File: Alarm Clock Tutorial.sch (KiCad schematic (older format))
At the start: 19 parts, among them K1 DIP-SWITCH-TACTILE-SPST-NO_TS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, K2 DIP-SWITCH-TACTILE-SPST-NO_TS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, K3 DIP-SWITCH-TACTILE-SPST-NO_TS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, U1 MCU-ATMEGA32U4-AU_TQFP44_, U2 LED-4-BETY-7-SEG_2X7P-30X14MM_

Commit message: First version fully routed
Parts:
- added BUZ1: DIP-BUZZER-3V_KS-12065D03YA_, SeeedOPL-Connector-2016:BZ2-7.6-D12.0XH6.5MM, symbol DIP-BUZZER-3V_KS-12065D03YA_
- added R12: DIP-RES-100R-5%-1_4W_PR-D2.3XL6.5MM_, SeeedOPL-Resistor-2016:PR-D2.3XL6.5MM, symbol DIP-RES-100R-5%-1_4W_PR-D2.3XL6.5MM_
- C1: footprint (none) -> SeeedOPL-Capacitor-2016:C1206
- C2: footprint (none) -> SeeedOPL-Capacitor-2016:C0805
- K1, K2, K3: footprint (none) -> SeeedOPL-Switch-2016:SW4-6.0X6.0X5.0MM
- R1, R10, R11, R2, R4, R5, R6, R7, R8, R9: footprint (none) -> SeeedOPL-Resistor-2016:R0805
- R3: footprint (none) -> SeeedOPL-Resistor-2016:R0402
- U1: footprint (none) -> SeeedOPL-IC-2016:TQFP44-0.8-9.6X9.6MM
- U2: footprint (none) -> SeeedOPL-Display-2016:LCD12-2.54-30.0X14.0X7.3MM
- USB1: footprint (none) -> SeeedOPL-Connector-2016:MICRO-USB5+6P-SMD-0.65-B
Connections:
- wire segments 81 -> 85
- no-connect marks 22 -> 21

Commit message: This version was ordered from Seeed Studio
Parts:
- added C3, C4: 12-22pF, SeeedOPL-Capacitor-2016:CERAMIC-2.54, symbol DIP-CERAMIC-DISC-100NF-50V-Y5V_D5.0MM_
- added Y1: 8-16 MHZ, SeeedOPL-Crystal Oscillator-2016:HC49US, symbol DIP-CRYSTAL-16MHZ-18PF-30PPM-40R_HC49US_
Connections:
- wire segments 85 -> 93
- no-connect marks 21 -> 19
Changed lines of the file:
@@
 LIBS:SeeedOPL-Resistor-2016
 LIBS:SeeedOPL-Switch-2016
+LIBS:SeeedOPL-Crystal Oscillator-2016
 LIBS:Alarm Clock Tutorial-cache
 EELAYER 25 0
@@
 NoConn ~ 4550 3050
 NoConn ~ 2100 4000
-NoConn ~ 4550 4350
-NoConn ~ 4550 4550
 NoConn ~ 4550 4750
 NoConn ~ 7050 5350
@@
 Wire Wire Line
 	2950 4850 3050 4850
+$Comp
+L DIP-CRYSTAL-16MHZ-18PF-30PPM-40R_HC49US_ Y1
+U 1 1 5A53881C
+P 4100 4450
+F 0 "Y1" H 4000 4550 45  0000 L BNN
+F 1 "8-16 MHZ" H 4000 4300 45  0000 L BNN
+F 2 "SeeedOPL-Crystal Oscillator-2016:HC49US" H 4100 4450 60  0001 C CNN
+F 3 "" H 4100 4450 60  0001 C CNN
+F 4 "306010014" H 4130 4600 20  0001 C CNN "SKU"
+	1    4100 4450
+	0    1    1    0
+$EndComp
+Wire Wire Line
+	3800 4600 4550 4600
+Wire Wire Line
+	4550 4600 4550 4550
+Wire Wire Line
+	3800 4300 4550 4300
+Wire Wire Line
+	4550 4300 4550 4350
+$Comp
+L DIP-CERAMIC-DISC-100NF-50V-Y5V_D5.0MM_ C3
+U 1 1 5A538B84
+P 3650 4300
+F 0 "C3" H 3500 4350 45  0000 L BNN
+F 1 "12-22pF" H 3500 4200 45  0000 L BNN
+F 2 "SeeedOPL-Capacitor-2016:CERAMIC-2.54" H 3650 4300 60  0001 C CNN
+F 3 "" H 3650 4300 60  0001 C CNN
+	1    3650 4300
+	1    0    0    -1
+$EndComp
+$Comp
+L DIP-CERAMIC-DISC-100NF-50V-Y5V_D5.0MM_ C4
+U 1 1 5A538C56
+P 3650 4600
+F 0 "C4" H 3500 4650 45  0000 L BNN
+F 1 "12-22pF" H 3500 4500 45  0000 L BNN
+F 2 "SeeedOPL-Capacitor-2016:CERAMIC-2.54" H 3650 4600 60  0001 C CNN
+F 3 "" H 3650 4600 60  0001 C CNN
+	1    3650 4600
+	1    0    0    -1
+$EndComp
+Connection ~ 4100 4600
+Connection ~ 4100 4300
+Wire Wire Line
+	3500 4600 3450 4600
+Wire Wire Line
+	3450 4600 3450 4300
+Wire Wire Line
+	3150 4300 3500 4300
+Wire Wire Line
+	3150 4300 3150 4450
+Connection ~ 3450 4300
+$Comp
+L GND #PWR014
+U 1 1 5A538F5F
+P 3150 4450
+F 0 "#PWR014" H 3150 4200 50  0001 C CNN
+F 1 "GND" H 3150 4300 50  0000 C CNN
+F 2 "" H 3150 4450 50  0001 C CNN
+F 3 "" H 3150 4450 50  0001 C CNN
+	1    3150 4450
+	1    0    0    -1
+$EndComp
 $EndSCHEMATC

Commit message: Updated part number for 7-segment
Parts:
- U2: MPN SYD3642ASR -> LDQ-N3606RI; SKU 304080005 -> (none)
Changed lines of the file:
@@
 F 2 "SeeedOPL-Display-2016:LCD12-2.54-30.0X14.0X7.3MM" H 8250 1950 60  0001 C CNN
 F 3 "" H 8250 1950 60  0001 C CNN
-F 4 "SYD3642ASR" H 8280 2100 20  0001 C CNN "MPN"
-F 5 "304080005" H 8280 2100 20  0001 C CNN "SKU"
+F 4 "LDQ-N3606RI" H 8280 2100 20  0001 C CNN "MPN"
 	1    8250 1950
 	1    0    0    -1

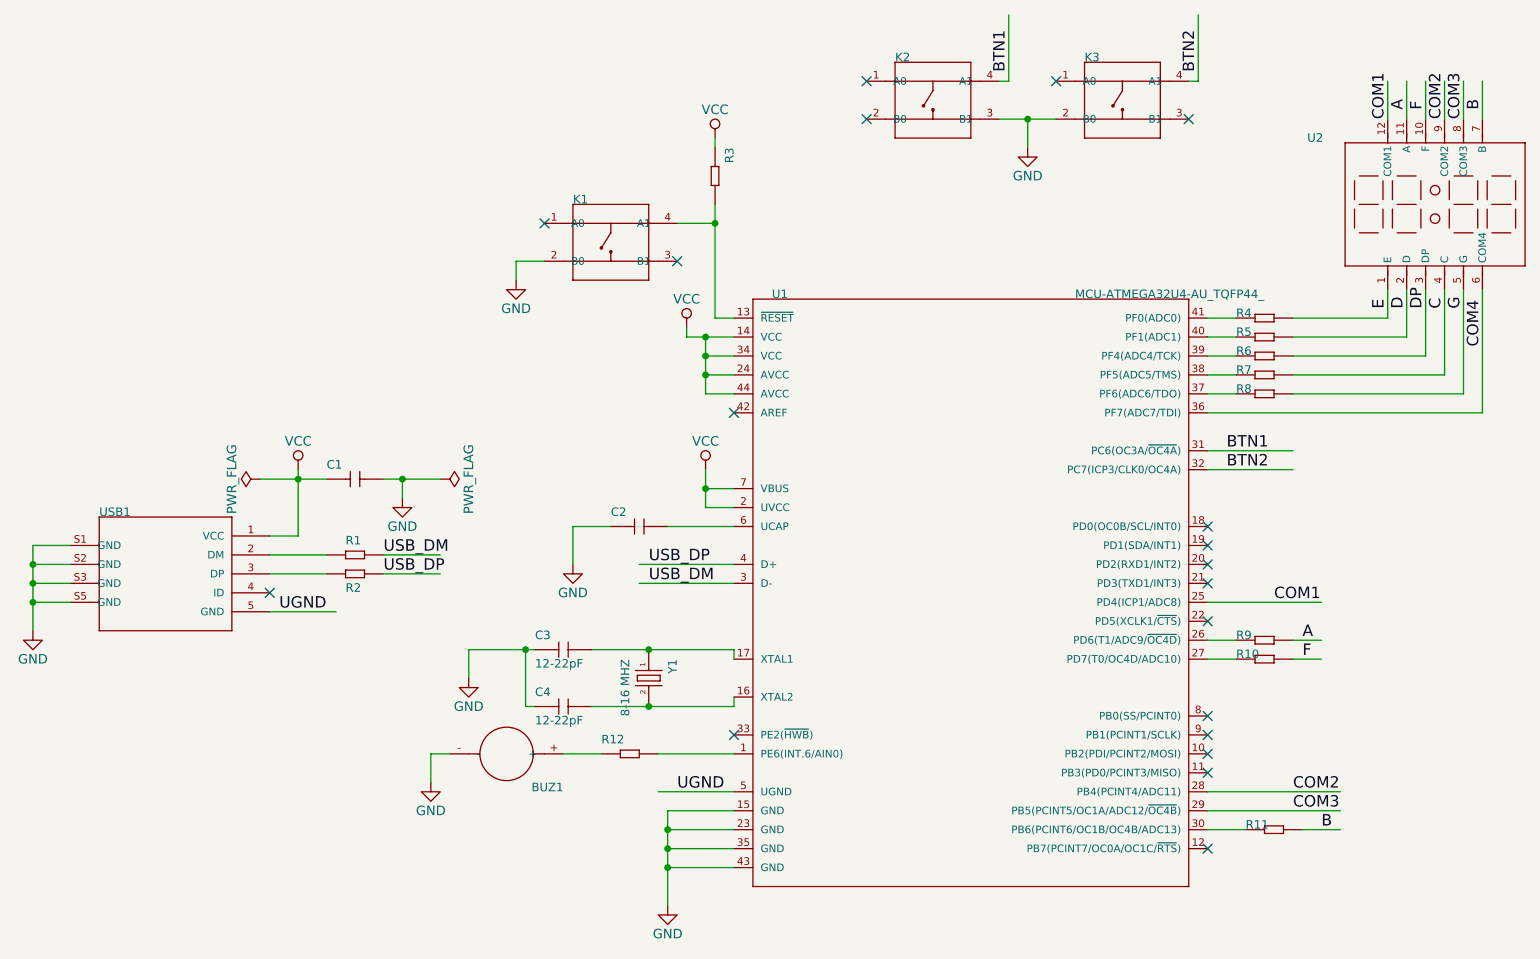
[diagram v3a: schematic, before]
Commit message: Updated component values on board
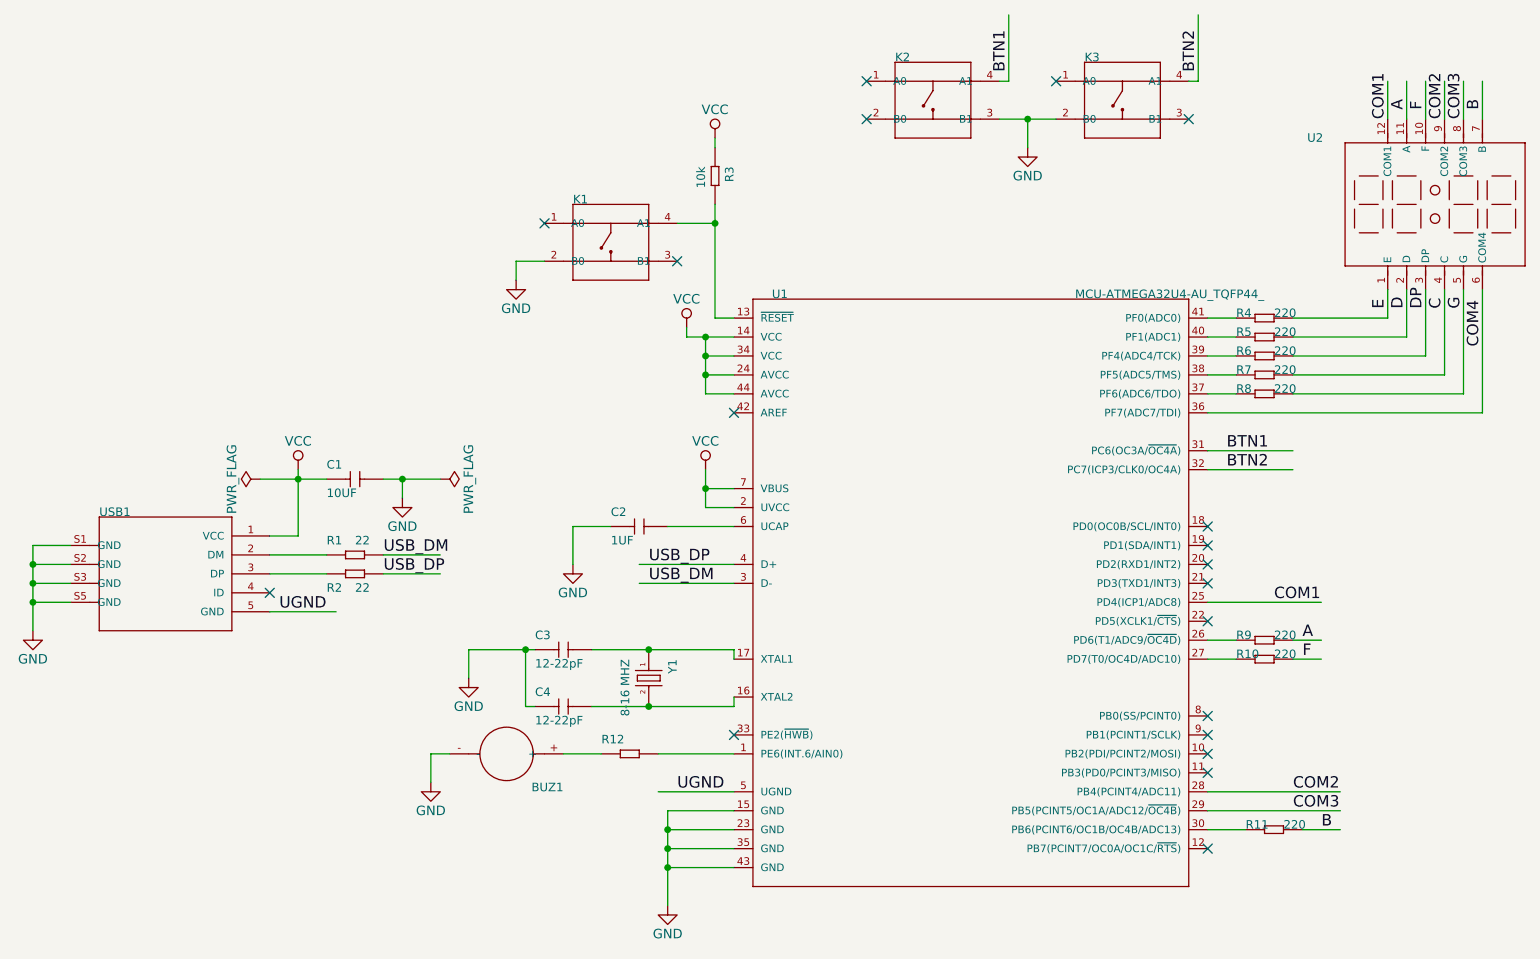
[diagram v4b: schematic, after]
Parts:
- C1: value CERAMIC-10UF-25V-10%-X5R_1206_ -> 10UF
- C2: value CERAMIC-1UF-25V-10%-X7R_0805_ -> 1UF
- R1, R2: value SMD-RES-22R-5%-1_8W_0805_ -> 22
- R10, R11, R4, R5, R6, R7, R8, R9: value SMD-RES-220R-5%-1_8W_0805_ -> 220
- R3: value SMD-RES-10K-1%-1_16W_0402_ -> 10k
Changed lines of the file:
@@
 U 1 1 5A4F7863
 P 2550 3800
-F 0 "R1" H 2500 3850 45  0000 L BNN
-F 1 "SMD-RES-22R-5%-1_8W_0805_" H 2400 3700 45  0001 L BNN
+F 0 "R1" H 2400 3850 45  0000 L BNN
+F 1 "22" H 2550 3850 45  0000 L BNN
 F 2 "SeeedOPL-Resistor-2016:R0805" H 2550 3800 40  0001 C CNN
 F 3 "" H 2550 3800 40  0001 C CNN
@@
 U 1 1 5A4F789F
 P 2550 3900
-F 0 "R2" H 2500 3800 45  0000 L BNN
-F 1 "SMD-RES-22R-5%-1_8W_0805_" H 2400 3800 45  0001 L BNN
+F 0 "R2" H 2400 3800 45  0000 L BNN
+F 1 "22" H 2550 3800 45  0000 L BNN
 F 2 "SeeedOPL-Resistor-2016:R0805" H 2550 3900 40  0001 C CNN
 F 3 "" H 2550 3900 40  0001 C CNN
@@
 P 7350 2550
 F 0 "R4" H 7200 2550 45  0000 L BNN
-F 1 "SMD-RES-220R-5%-1_8W_0805_" H 7200 2450 45  0001 L BNN
+F 1 "220" H 7400 2550 45  0000 L BNN
 F 2 "SeeedOPL-Resistor-2016:R0805" H 7350 2550 40  0001 C CNN
 F 3 "" H 7350 2550 40  0001 C CNN
@@
 P 7350 2650
 F 0 "R5" H 7200 2650 45  0000 L BNN
-F 1 "SMD-RES-220R-5%-1_8W_0805_" H 7200 2550 45  0001 L BNN
+F 1 "220" H 7400 2650 45  0000 L BNN
 F 2 "SeeedOPL-Resistor-2016:R0805" H 7350 2650 40  0001 C CNN
 F 3 "" H 7350 2650 40  0001 C CNN
@@
 P 7350 2750
 F 0 "R6" H 7200 2750 45  0000 L BNN
-F 1 "SMD-RES-220R-5%-1_8W_0805_" H 7200 2650 45  0001 L BNN
+F 1 "220" H 7400 2750 45  0000 L BNN
 F 2 "SeeedOPL-Resistor-2016:R0805" H 7350 2750 40  0001 C CNN
 F 3 "" H 7350 2750 40  0001 C CNN
@@
 P 7350 2850
 F 0 "R7" H 7200 2850 45  0000 L BNN
-F 1 "SMD-RES-220R-5%-1_8W_0805_" H 7200 2750 45  0001 L BNN
+F 1 "220" H 7400 2850 45  0000 L BNN
 F 2 "SeeedOPL-Resistor-2016:R0805" H 7350 2850 40  0001 C CNN
 F 3 "" H 7350 2850 40  0001 C CNN
@@
 P 7350 2950
 F 0 "R8" H 7200 2950 45  0000 L BNN
-F 1 "SMD-RES-220R-5%-1_8W_0805_" H 7200 2850 45  0001 L BNN
+F 1 "220" H 7400 2950 45  0000 L BNN
 F 2 "SeeedOPL-Resistor-2016:R0805" H 7350 2950 40  0001 C CNN
 F 3 "" H 7350 2950 40  0001 C CNN
@@
 P 7400 5250
 F 0 "R11" H 7250 5250 45  0000 L BNN
-F 1 "SMD-RES-220R-5%-1_8W_0805_" H 7250 5150 45  0001 L BNN
+F 1 "220" H 7450 5250 45  0000 L BNN
 F 2 "SeeedOPL-Resistor-2016:R0805" H 7400 5250 40  0001 C CNN
 F 3 "" H 7400 5250 40  0001 C CNN
@@
 P 7350 4350
 F 0 "R10" H 7200 4350 45  0000 L BNN
-F 1 "SMD-RES-220R-5%-1_8W_0805_" H 7200 4250 45  0001 L BNN
+F 1 "220" H 7400 4350 45  0000 L BNN
 F 2 "SeeedOPL-Resistor-2016:R0805" H 7350 4350 40  0001 C CNN
 F 3 "" H 7350 4350 40  0001 C CNN
@@
 P 7350 4250
 F 0 "R9" H 7200 4250 45  0000 L BNN
-F 1 "SMD-RES-220R-5%-1_8W_0805_" H 7200 4150 45  0001 L BNN
+F 1 "220" H 7400 4250 45  0000 L BNN
 F 2 "SeeedOPL-Resistor-2016:R0805" H 7350 4250 40  0001 C CNN
 F 3 "" H 7350 4250 40  0001 C CNN
@@
 U 1 1 5A4FB126
 P 4450 1800
-F 0 "R3" H 4300 1850 45  0000 L BNN
-F 1 "SMD-RES-10K-1%-1_16W_0402_" H 4300 1700 45  0001 L BNN
+F 0 "R3" H 4400 1850 45  0000 L BNN
+F 1 "10k" H 4400 1700 45  0000 L BNN
 F 2 "SeeedOPL-Resistor-2016:R0402" H 4450 1800 40  0001 C CNN
 F 3 "" H 4450 1800 40  0001 C CNN
@@
 P 2550 3400
 F 0 "C1" H 2400 3450 45  0000 L BNN
-F 1 "CERAMIC-10UF-25V-10%-X5R_1206_" H 2400 3300 45  0001 L BNN
+F 1 "10UF" H 2400 3300 45  0000 L BNN
 F 2 "SeeedOPL-Capacitor-2016:C1206" H 2550 3400 60  0001 C CNN
 F 3 "" H 2550 3400 60  0001 C CNN
@@
 P 4050 3650
 F 0 "C2" H 3900 3700 45  0000 L BNN
-F 1 "CERAMIC-1UF-25V-10%-X7R_0805_" H 3900 3550 45  0001 L BNN
+F 1 "1UF" H 3900 3550 45  0000 L BNN
 F 2 "SeeedOPL-Capacitor-2016:C0805" H 4050 3650 60  0001 C CNN
 F 3 "" H 4050 3650 60  0001 C CNN
